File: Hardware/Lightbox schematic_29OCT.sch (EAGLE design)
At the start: 8 parts, among them IC2 7805T, U1 ARDUINOR3-DIMENSION

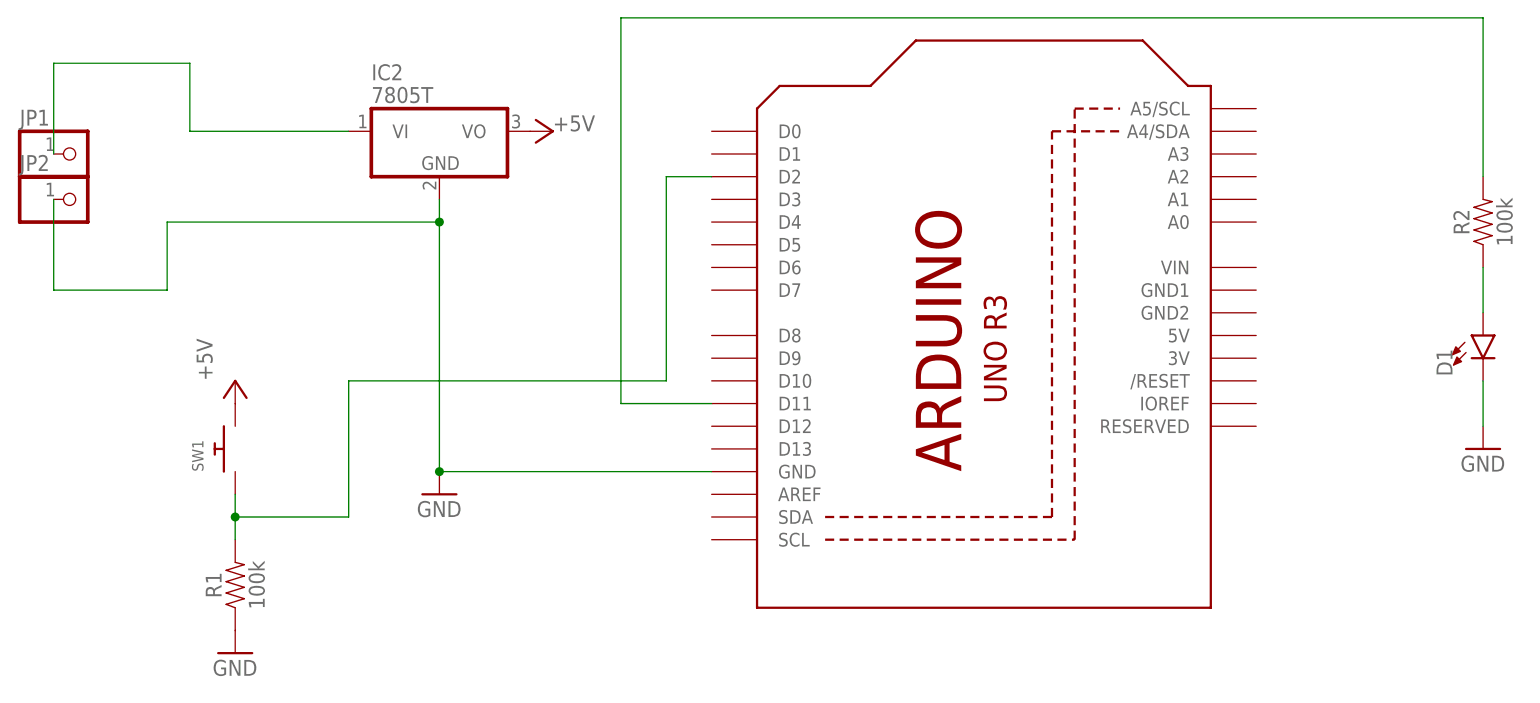
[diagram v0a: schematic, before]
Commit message: add revs of schematic/PCB iterated on in office
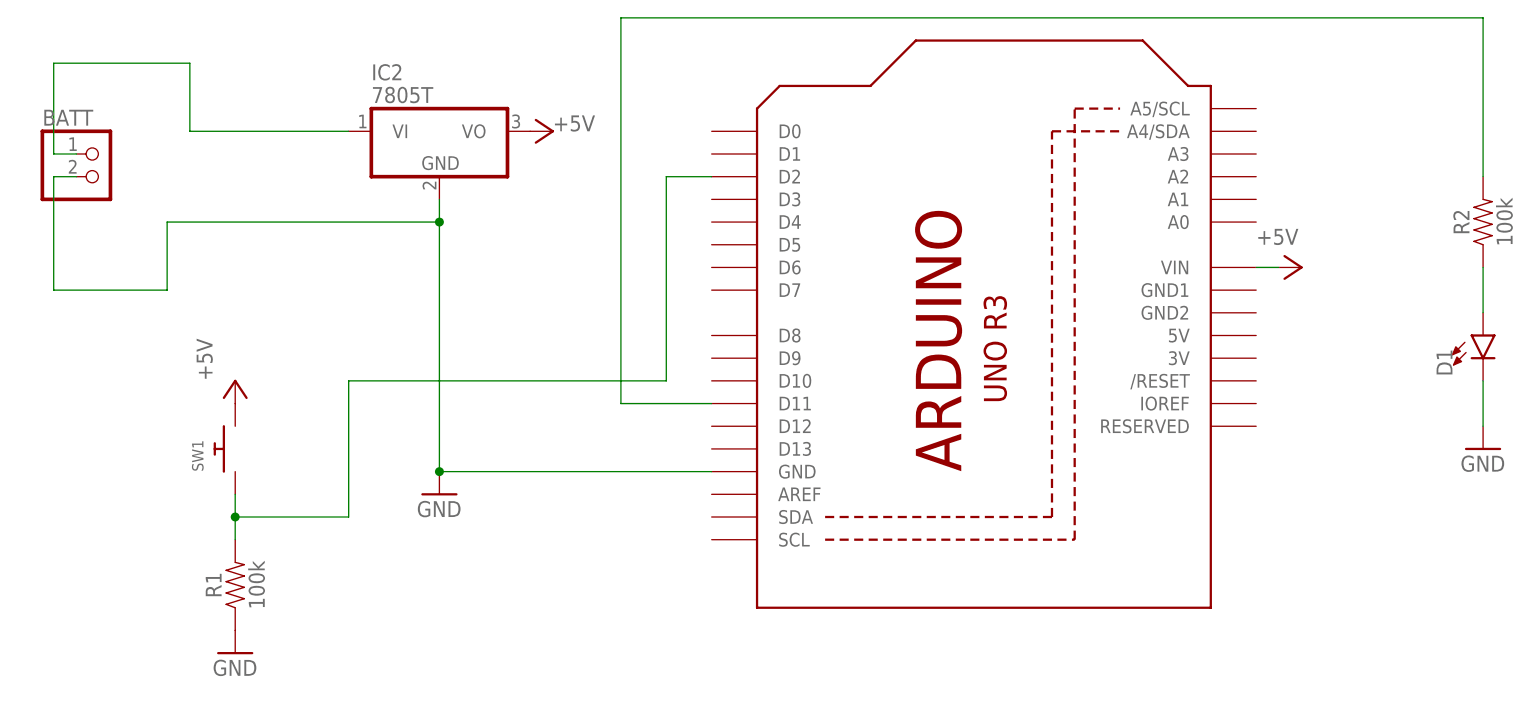
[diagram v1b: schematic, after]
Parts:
- removed JP1, JP2: (no value), adafruit:PINHD-1X1
- added BATT: (no value), pinhead:PINHD-1X2
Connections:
- removed net N$1: IC2.VI, JP1.1
- new net BATT: BATT.1, IC2.VI
- net +5V: now also U1.VIN
- net GND: now also BATT.2; no longer JP2.1
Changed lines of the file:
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@@
 <?xml version="1.0" encoding="utf-8"?>
 <!DOCTYPE eagle SYSTEM "eagle.dtd">
-<eagle version="9.2.0">
+<eagle version="9.2.2">
 <drawing>
 <settings>
@@
 <part name="GND2" library="supply1" library_urn="urn:adsk.eagle:library:371" deviceset="GND" device=""/>
 <part name="GND3" library="supply1" library_urn="urn:adsk.eagle:library:371" deviceset="GND" device=""/>
-<part name="JP1" library="adafruit" library_urn="urn:adsk.eagle:library:420" deviceset="PINHD-1X1" device="" package3d_urn="urn:adsk.eagle:package:6240654/1"/>
-<part name="JP2" library="adafruit" library_urn="urn:adsk.eagle:library:420" deviceset="PINHD-1X1" device="" package3d_urn="urn:adsk.eagle:package:6240654/1"/>
+<part name="P+3" library="supply1" library_urn="urn:adsk.eagle:library:371" deviceset="+5V" device=""/>
+<part name="BATT" library="pinhead" library_urn="urn:adsk.eagle:library:325" deviceset="PINHD-1X2" device="" package3d_urn="urn:adsk.eagle:package:22435/2"/>
 </parts>
 <sheets>
@@
 </plain>
 <instances>
-<instance part="IC2" gate="A1" x="35.56" y="83.82">
+<instance part="IC2" gate="A1" x="35.56" y="83.82" smashed="yes">
 <attribute name="NAME" x="27.94" y="89.535" size="1.778" layer="95"/>
 <attribute name="VALUE" x="27.94" y="86.995" size="1.778" layer="96"/>
 </instance>
-<instance part="R1" gate="G$1" x="12.7" y="33.02" rot="R90">
+<instance part="R1" gate="G$1" x="12.7" y="33.02" smashed="yes" rot="R90">
 <attribute name="NAME" x="11.176" y="33.02" size="1.778" layer="95" font="vector" rot="R90" align="bottom-center"/>
 <attribute name="VALUE" x="14.224" y="33.02" size="1.778" layer="96" font="vector" rot="R90" align="top-center"/>
 </instance>
-<instance part="D1" gate="G$1" x="152.4" y="60.96">
+<instance part="D1" gate="G$1" x="152.4" y="60.96" smashed="yes">
 <attribute name="NAME" x="148.971" y="56.388" size="1.778" layer="95" font="vector" rot="R90"/>
 <attribute name="VALUE" x="154.305" y="56.388" size="1.778" layer="96" font="vector" rot="R90" align="top-left"/>
 </instance>
-<instance part="U1" gate="G$1" x="96.52" y="63.5" rot="R90"/>
-<instance part="R2" gate="G$1" x="152.4" y="73.66" rot="R90">
+<instance part="U1" gate="G$1" x="96.52" y="63.5" smashed="yes" rot="R90"/>
+<instance part="R2" gate="G$1" x="152.4" y="73.66" smashed="yes" rot="R90">
 <attribute name="NAME" x="150.876" y="73.66" size="1.778" layer="95" font="vector" rot="R90" align="bottom-center"/>
 <attribute name="VALUE" x="153.924" y="73.66" size="1.778" layer="96" font="vector" rot="R90" align="top-center"/>
 </instance>
-<instance part="SW1" gate="G$1" x="12.7" y="48.26" rot="R90">
+<instance part="SW1" gate="G$1" x="12.7" y="48.26" smashed="yes" rot="R90">
 <attribute name="NAME" x="9.144" y="45.72" size="1.27" layer="95" rot="R90"/>
 <attribute name="VALUE" x="14.986" y="45.72" size="1.27" layer="96" rot="R90"/>
 </instance>
-<instance part="P+1" gate="1" x="48.26" y="83.82" rot="R270">
+<instance part="P+1" gate="1" x="48.26" y="83.82" smashed="yes" rot="R270">
 <attribute name="VALUE" x="48.26" y="83.82" size="1.778" layer="96"/>
 </instance>
-<instance part="P+2" gate="1" x="12.7" y="55.88">
+<instance part="P+2" gate="1" x="12.7" y="55.88" smashed="yes">
 <attribute name="VALUE" x="10.16" y="55.88" size="1.778" layer="96" rot="R90"/>
 </instance>
-<instance part="GND1" gate="1" x="12.7" y="25.4">
+<instance part="GND1" gate="1" x="12.7" y="25.4" smashed="yes">
 <attribute name="VALUE" x="10.16" y="22.86" size="1.778" layer="96"/>
 </instance>
-<instance part="GND2" gate="1" x="35.56" y="43.18">
+<instance part="GND2" gate="1" x="35.56" y="43.18" smashed="yes">
 <attribute name="VALUE" x="33.02" y="40.64" size="1.778" layer="96"/>
 </instance>
-<instance part="GND3" gate="1" x="152.4" y="48.26">
+<instance part="GND3" gate="1" x="152.4" y="48.26" smashed="yes">
 <attribute name="VALUE" x="149.86" y="45.72" size="1.778" layer="96"/>
 </instance>
-<instance part="JP1" gate="G$1" x="-5.08" y="81.28">
-<attribute name="NAME" x="-11.43" y="84.455" size="1.778" layer="95"/>
-<attribute name="VALUE" x="-11.43" y="76.2" size="1.778" layer="96"/>
-</instance>
-<instance part="JP2" gate="G$1" x="-5.08" y="76.2">
-<attribute name="NAME" x="-11.43" y="79.375" size="1.778" layer="95"/>
-<attribute name="VALUE" x="-11.43" y="71.12" size="1.778" layer="96"/>
+<instance part="P+3" gate="1" x="132.08" y="68.58" smashed="yes" rot="R270">
+<attribute name="VALUE" x="127" y="71.12" size="1.778" layer="96"/>
+</instance>
+<instance part="BATT" gate="G$1" x="-2.54" y="78.74" smashed="yes">
+<attribute name="NAME" x="-8.89" y="84.455" size="1.778" layer="95"/>
+<attribute name="VALUE" x="-8.89" y="73.66" size="1.778" layer="96"/>
 </instance>
 </instances>
@@
 </busses>
 <nets>
-<net name="N$1" class="0">
+<net name="BATT" class="0">
 <segment>
 <wire x1="7.62" y1="83.82" x2="25.4" y2="83.82" width="0.1524" layer="91"/>
@@
 <wire x1="-7.62" y1="91.44" x2="7.62" y2="91.44" width="0.1524" layer="91"/>
 <wire x1="7.62" y1="91.44" x2="7.62" y2="83.82" width="0.1524" layer="91"/>
-<pinref part="JP1" gate="G$1" pin="1"/>
 <wire x1="-7.62" y1="91.44" x2="-7.62" y2="81.28" width="0.1524" layer="91"/>
+<pinref part="BATT" gate="G$1" pin="1"/>
+<wire x1="-5.08" y1="81.28" x2="-7.62" y2="81.28" width="0.1524" layer="91"/>
 </segment>
 </net>
@@
 <pinref part="GND2" gate="1" pin="GND"/>
 <junction x="35.56" y="45.72"/>
-<pinref part="JP2" gate="G$1" pin="1"/>
-<wire x1="-7.62" y1="76.2" x2="-7.62" y2="66.04" width="0.1524" layer="91"/>
+<wire x1="-7.62" y1="78.74" x2="-7.62" y2="66.04" width="0.1524" layer="91"/>
+<pinref part="BATT" gate="G$1" pin="2"/>
+<wire x1="-5.08" y1="78.74" x2="-7.62" y2="78.74" width="0.1524" layer="91"/>
 </segment>
 <segment>
@@
 <pinref part="P+1" gate="1" pin="+5V"/>
 </segment>
-</net>
+<segment>
+<pinref part="U1" gate="G$1" pin="VIN"/>
+<pinref part="P+3" gate="1" pin="+5V"/>
+<wire x1="127" y1="68.58" x2="129.54" y2="68.58" width="0.1524" layer="91"/>
+</segment>
+</net>
